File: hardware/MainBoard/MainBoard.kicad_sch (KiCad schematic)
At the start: 22 parts, among them J1 Therm., J2 SSR, J3 Serial, J4 5Vin, J6 Keypad1, SW1 Boot Mode, SW2 RESET, U1 ESP-12F, U2 AMS1117-3.3

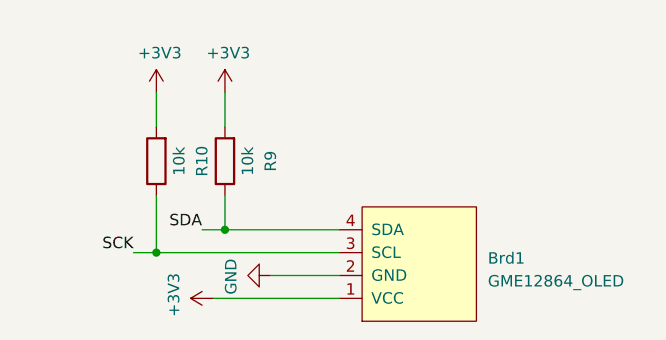
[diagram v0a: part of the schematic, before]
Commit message: gme12864 replaced with ssd1306
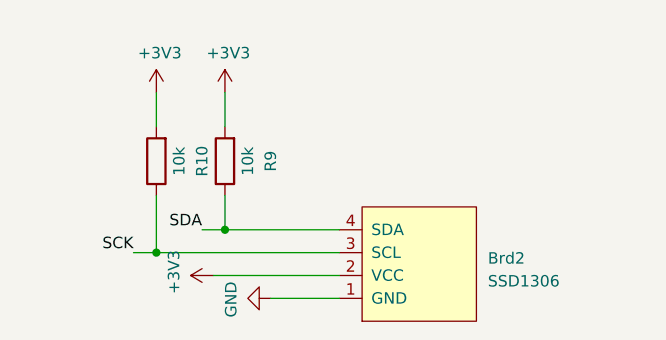
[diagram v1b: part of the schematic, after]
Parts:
- removed Brd1: GME12864_OLED, SSD1306:GME12864_OLED, symbol SSD1306-128x64_OLED:GME12864_OLED
- removed U1: ESP-12F, RF_Module:ESP-07, symbol ESP8266:ESP-12E
- added Brd2: SSD1306, SSD1306:128x64OLED, symbol SSD1306-128x64_OLED:SSD1306
- added U1: ESP-12F, ESP8266:ESP-07-RF_Modules, symbol ESP8266:ESP-12F
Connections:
- net +3V3: now also Brd2.2 (VCC), U1.3 (CH_PD), U1.8 (VCC)
- net A0: now also U1.2 (ADC)
- net GND: now also Brd2.1 (GND), U1.9 (GND)
- net IO00: now also U1.12 (GPIO0)
- net IO02: now also U1.11 (GPIO2)
- net IO12: now also U1.6 (GPIO12)
- net IO13: now also U1.7 (GPIO13)
- net IO14: now also U1.5 (GPIO14)
- net IO16: now also U1.4 (GPIO16)
- net RESET: now also U1.1 (REST)
- net RX: now also U1.15 (RXD)
- net SCK: now also Brd2.3 (SCL), U1.14 (GPIO5)
- net SDA: now also Brd2.4 (SDA), U1.13 (GPIO4)
- net TX: now also U1.16 (TXD)

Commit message: libraries updated
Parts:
- removed Brd2: SSD1306, SSD1306:128x64OLED, symbol SSD1306-128x64_OLED:SSD1306
- added Brd1: SSD1306, SSD1306:128x64OLED, symbol SSD1306-128x64_OLED:SSD1306
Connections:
- net +3V3: now also Brd1.2 (VCC)
- net GND: now also Brd1.1 (GND)
- net SCK: now also Brd1.3 (SCL)
- net SDA: now also Brd1.4 (SDA)

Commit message: redesign pcb files
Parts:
- removed Brd1: SSD1306, SSD1306:128x64OLED, symbol SSD1306-128x64_OLED:SSD1306
- added J5: LCD, Connector_PinHeader_2.54mm:PinHeader_1x04_P2.54mm_Vertical, symbol Connector:Conn_01x04_Pin
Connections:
- net +3V3: now also J5.2 (Pin_2)
- net GND: now also J5.1 (Pin_1)
- net SCK: now also J5.3 (Pin_3)
- net SDA: now also J5.4 (Pin_4)
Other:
- note added: "Keypad w. LCD Module"
- moved on the sheet: J6, R10, R9
